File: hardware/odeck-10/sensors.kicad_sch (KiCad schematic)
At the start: 0 parts

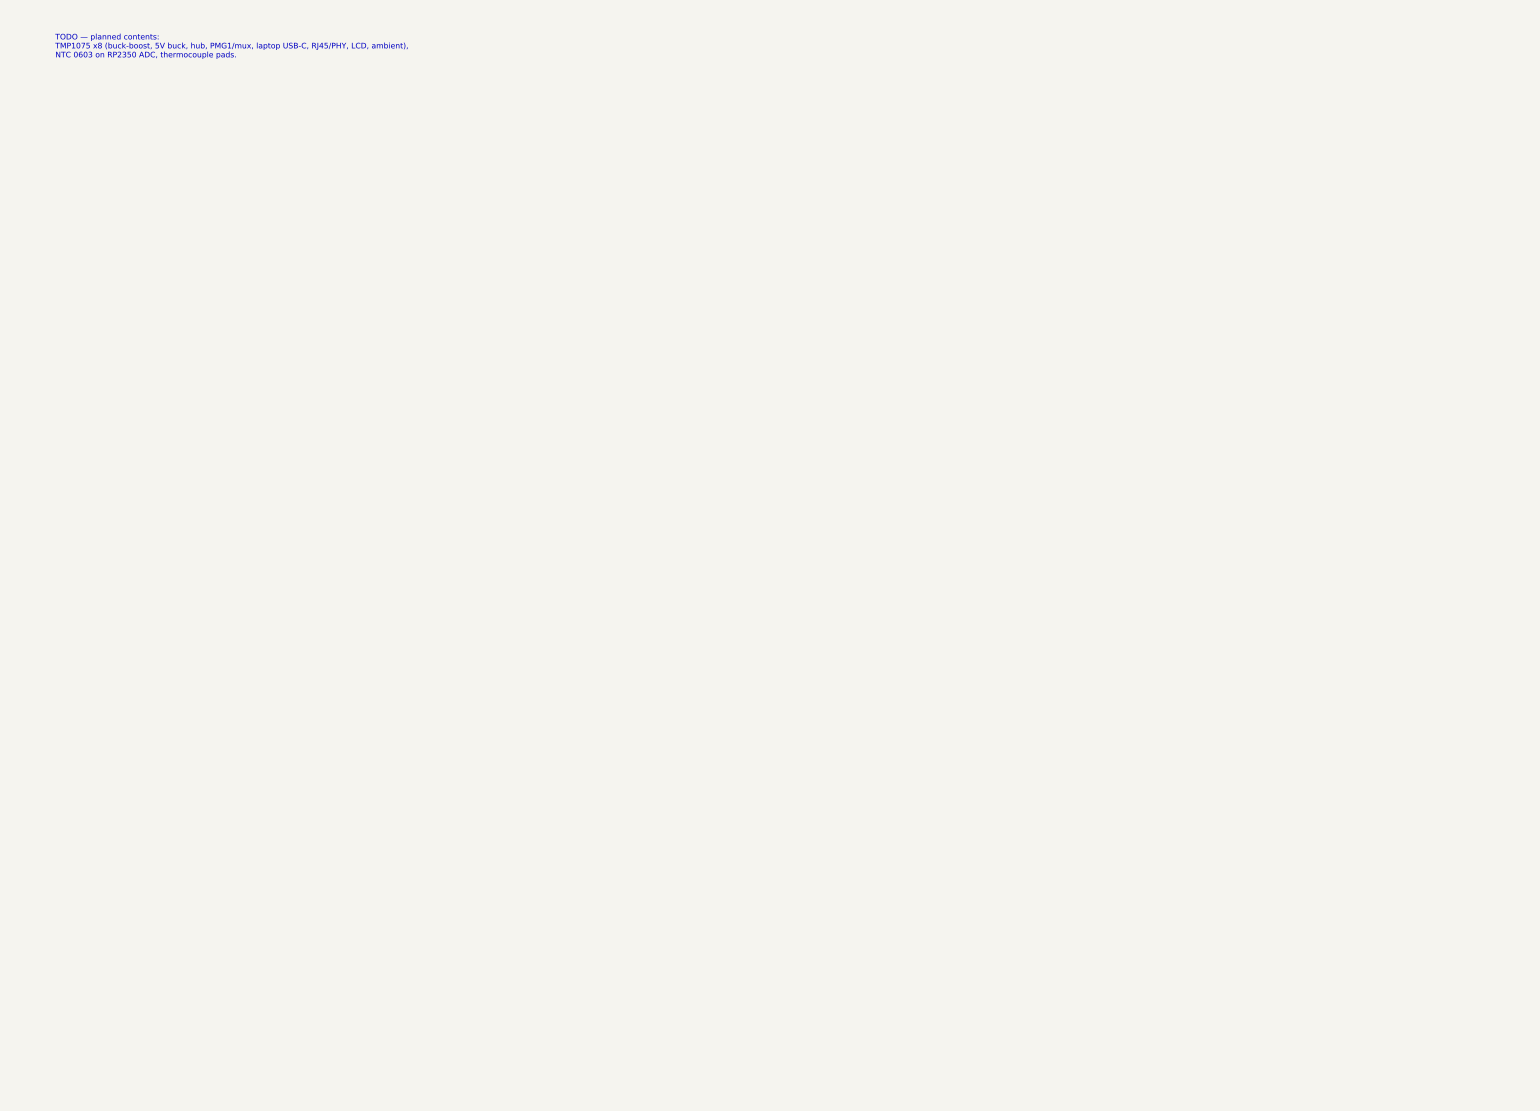
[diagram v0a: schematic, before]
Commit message: Draft remaining sheets: USB-A, card reader, Ethernet, MCU, display/UI, sensors
- usb_a: 2x 10G USB-A, TPS2553 switches (hub OR RP2350 force), INA180 sense
- card_reader: GL3224 + SD/microSD, card detect + activity to MCU
- ethernet: RTL8156BG with switched 3.3 V, 0.95 V PWM buck, 2.5G magjack,
  LED buffer, EUI-48 EEPROM + gated I2C bridge for MAC eFuse write
- mcu: RP2350B reference core, full GPIO table, TCA9534 expander, PIO I2C
- display_ui: 2.0" ST7789 LCD + backlight PWM, buttons, unpopulated GPIO
  header (series R + ESD), Qwiic
- sensors: 8x TMP1075, 2 NTCs, thermocouple pads
- integration: ETH_I2C_EN net, TPS62933F for +3V3, PWR_FLAGs
- schgen: deterministic UUIDs; bom_check: cost summary
- 181 parts, all JLC stock >= 5; netlist verify OK; ERC clean but 1 spare pin

Co-Authored-By: Claude Opus 5.5 <noreply@anthropic.com>
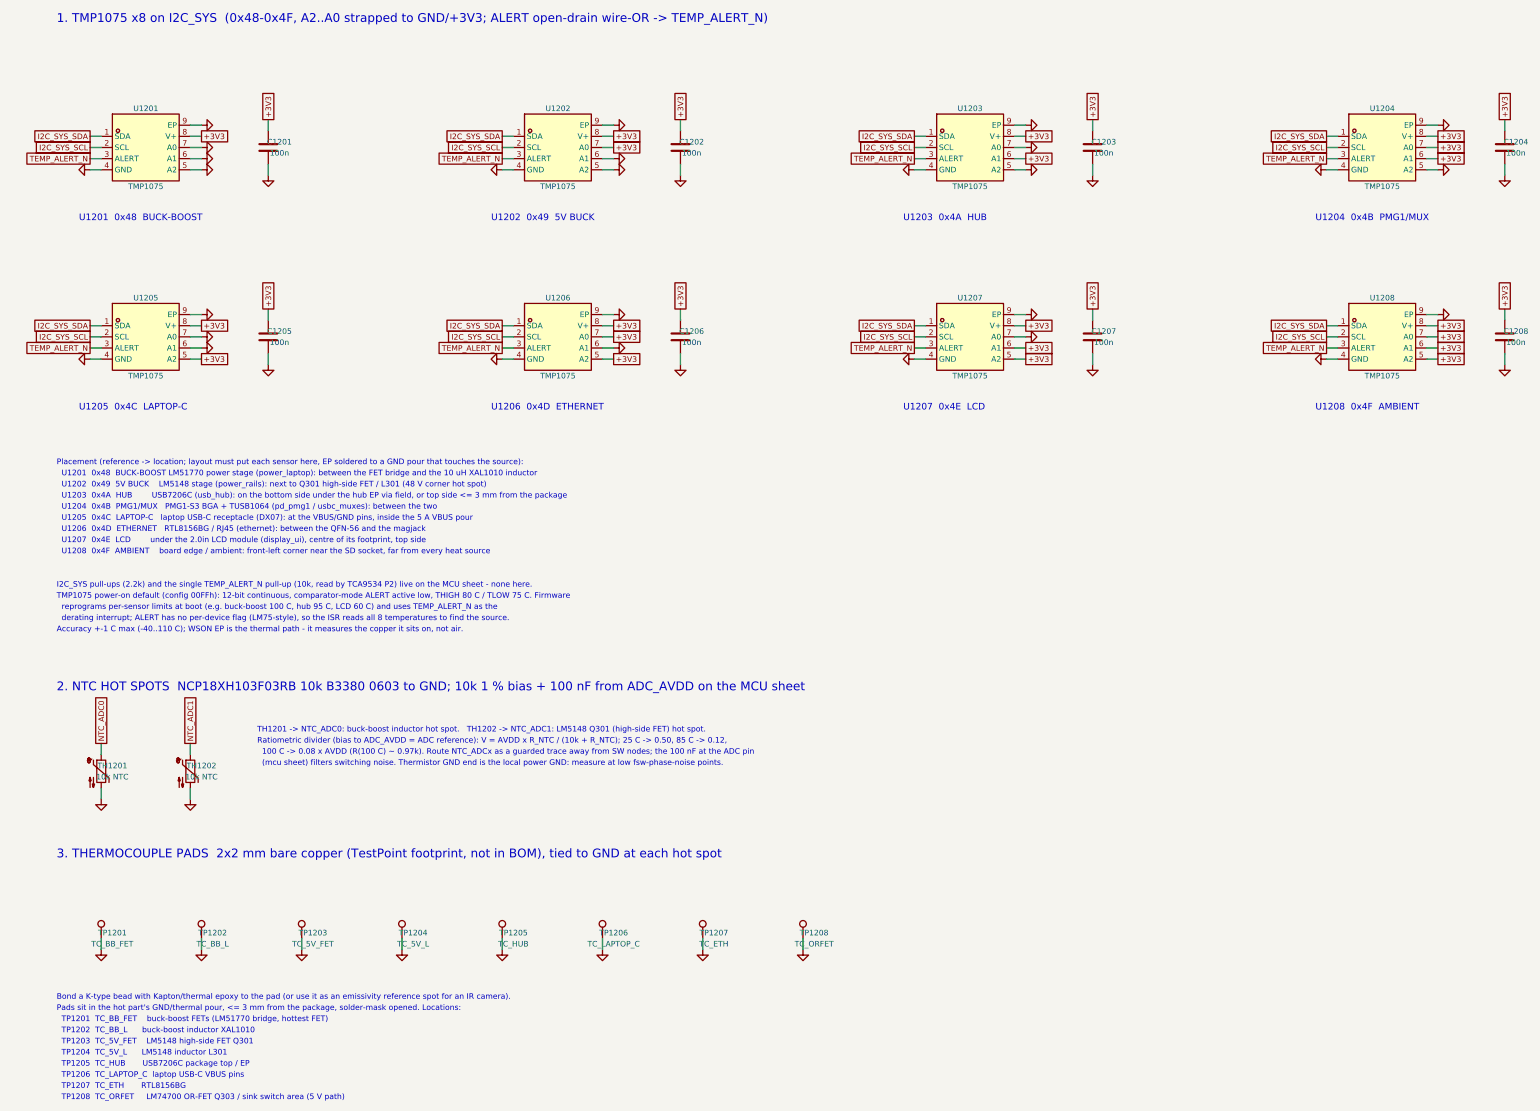
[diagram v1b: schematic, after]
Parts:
- added C1201, C1202, C1203, C1204, C1205, C1206, C1207, C1208: 100n, Capacitor_SMD:C_0402_1005Metric, symbol Device:C
- added TH1201, TH1202: 10k NTC, Resistor_SMD:R_0603_1608Metric, symbol Device:Thermistor_NTC
- added TP1201: TC_BB_FET, TestPoint:TestPoint_Pad_2.0x2.0mm, symbol Connector:TestPoint
- added TP1202: TC_BB_L, TestPoint:TestPoint_Pad_2.0x2.0mm, symbol Connector:TestPoint
- added TP1203: TC_5V_FET, TestPoint:TestPoint_Pad_2.0x2.0mm, symbol Connector:TestPoint
- added TP1204: TC_5V_L, TestPoint:TestPoint_Pad_2.0x2.0mm, symbol Connector:TestPoint
- added TP1205: TC_HUB, TestPoint:TestPoint_Pad_2.0x2.0mm, symbol Connector:TestPoint
- added TP1206: TC_LAPTOP_C, TestPoint:TestPoint_Pad_2.0x2.0mm, symbol Connector:TestPoint
- added TP1207: TC_ETH, TestPoint:TestPoint_Pad_2.0x2.0mm, symbol Connector:TestPoint
- added TP1208: TC_ORFET, TestPoint:TestPoint_Pad_2.0x2.0mm, symbol Connector:TestPoint
- added U1201, U1202, U1203, U1204, U1205, U1206, U1207, U1208: TMP1075, odeck:WSON-8_L2.0-W2.0-P0.50-TL-EP, symbol odeck:TMP1075DSGR
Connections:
- new net +3V3: C1201.1, C1202.1, C1203.1, C1204.1, C1205.1, C1206.1, C1207.1, C1208.1, U1201.8 (V+), U1202.7 (A0), U1202.8 (V+), U1203.6 (A1), U1203.8 (V+), U1204.6 (A1), U1204.7 (A0), U1204.8 (V+), U1205.5 (A2), U1205.8 (V+), U1206.5 (A2), U1206.7 (A0), U1206.8 (V+), U1207.5 (A2), U1207.6 (A1), U1207.8 (V+), U1208.5 (A2), U1208.6 (A1), U1208.7 (A0), U1208.8 (V+)
- new net GND: C1201.2, C1202.2, C1203.2, C1204.2, C1205.2, C1206.2, C1207.2, C1208.2, TH1201.2, TH1202.2, TP1201.1, TP1202.1, TP1203.1, TP1204.1, TP1205.1, TP1206.1, TP1207.1, TP1208.1, U1201.4 (GND), U1201.5 (A2), U1201.6 (A1), U1201.7 (A0), U1201.9 (EP), U1202.4 (GND), U1202.5 (A2), U1202.6 (A1), U1202.9 (EP), U1203.4 (GND), U1203.5 (A2), U1203.7 (A0), U1203.9 (EP), U1204.4 (GND), U1204.5 (A2), U1204.9 (EP), U1205.4 (GND), U1205.6 (A1), U1205.7 (A0), U1205.9 (EP), U1206.4 (GND), U1206.6 (A1), U1206.9 (EP), U1207.4 (GND), U1207.7 (A0), U1207.9 (EP), U1208.4 (GND), U1208.9 (EP)
- new net I2C_SYS_SCL: U1201.2 (SCL), U1202.2 (SCL), U1203.2 (SCL), U1204.2 (SCL), U1205.2 (SCL), U1206.2 (SCL), U1207.2 (SCL), U1208.2 (SCL)
- new net I2C_SYS_SDA: U1201.1 (SDA), U1202.1 (SDA), U1203.1 (SDA), U1204.1 (SDA), U1205.1 (SDA), U1206.1 (SDA), U1207.1 (SDA), U1208.1 (SDA)
- new net NTC_ADC0: TH1201.1
- new net NTC_ADC1: TH1202.1
- new net TEMP_ALERT_N: U1201.3 (ALERT), U1202.3 (ALERT), U1203.3 (ALERT), U1204.3 (ALERT), U1205.3 (ALERT), U1206.3 (ALERT), U1207.3 (ALERT), U1208.3 (ALERT)
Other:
- note added: "(mcu sheet) filters switching noise. Thermistor GND end is the local power GND: measure at low fsw-phase-noise points."
- note added: "1. TMP1075 x8 on I2C_SYS (0x48-0x4F, A2..A0 strapped to GND/+3V3; ALERT open-drain wire-OR -> TEMP_ALERT_N)"
- note added: "100 C -> 0.08 x AVDD (R(100 C) ~ 0.97k). Route NTC_ADCx as a guarded trace away from SW nodes; the 100 nF at the ADC pin"
- note added: "2. NTC HOT SPOTS NCP18XH103F03RB 10k B3380 0603 to GND; 10k 1 % bias + 100 nF from ADC_AVDD on the MCU sheet"
- note added: "3. THERMOCOUPLE PADS 2x2 mm bare copper (TestPoint footprint, not in BOM), tied to GND at each hot spot"
- note added: "Accuracy +-1 C max (-40..110 C); WSON EP is the thermal path - it measures the copper it sits on, not air."
- note added: "Bond a K-type bead with Kapton/thermal epoxy to the pad (or use it as an emissivity reference spot for an IR camera)."
- note added: "I2C_SYS pull-ups (2.2k) and the single TEMP_ALERT_N pull-up (10k, read by TCA9534 P2) live on the MCU sheet - none here."
- note added: "Pads sit in the hot part's GND/thermal pour, <= 3 mm from the package, solder-mask opened. Locations:"
- note added: "Placement (reference -> location; layout must put each sensor here, EP soldered to a GND pour that touches the source):"
- note added: "Ratiometric divider (bias to ADC_AVDD = ADC reference): V = AVDD x R_NTC / (10k + R_NTC); 25 C -> 0.50, 85 C -> 0.12,"
- note added: "TH1201 -> NTC_ADC0: buck-boost inductor hot spot. TH1202 -> NTC_ADC1: LM5148 Q301 (high-side FET) hot spot."
- note added: "TMP1075 power-on default (config 00FFh): 12-bit continuous, comparator-mode ALERT active low, THIGH 80 C / TLOW 75 C. Firmware"
- note added: "TP1201 TC_BB_FET buck-boost FETs (LM51770 bridge, hottest FET)"
- note added: "TP1202 TC_BB_L buck-boost inductor XAL1010"
- note added: "TP1203 TC_5V_FET LM5148 high-side FET Q301"
- note added: "TP1204 TC_5V_L LM5148 inductor L301"
- note added: "TP1205 TC_HUB USB7206C package top / EP"
- note added: "TP1206 TC_LAPTOP_C laptop USB-C VBUS pins"
- note added: "TP1207 TC_ETH RTL8156BG"
- note added: "TP1208 TC_ORFET LM74700 OR-FET Q303 / sink switch area (5 V path)"
- note added: "U1201 0x48 BUCK-BOOST"
- note added: "U1201 0x48 BUCK-BOOST LM51770 power stage (power_laptop): between the FET bridge and the 10 uH XAL1010 inductor"
- note added: "U1202 0x49 5V BUCK"
- note added: "U1202 0x49 5V BUCK LM5148 stage (power_rails): next to Q301 high-side FET / L301 (48 V corner hot spot)"
- note added: "U1203 0x4A HUB"
- note added: "U1203 0x4A HUB USB7206C (usb_hub): on the bottom side under the hub EP via field, or top side <= 3 mm from the package"
- note added: "U1204 0x4B PMG1/MUX"
- note added: "U1204 0x4B PMG1/MUX PMG1-S3 BGA + TUSB1064 (pd_pmg1 / usbc_muxes): between the two"
- note added: "U1205 0x4C LAPTOP-C"
- note added: "U1205 0x4C LAPTOP-C laptop USB-C receptacle (DX07): at the VBUS/GND pins, inside the 5 A VBUS pour"
- note added: "U1206 0x4D ETHERNET"
- note added: "U1206 0x4D ETHERNET RTL8156BG / RJ45 (ethernet): between the QFN-56 and the magjack"
- note added: "U1207 0x4E LCD"
- note added: "U1207 0x4E LCD under the 2.0in LCD module (display_ui), centre of its footprint, top side"
- note added: "U1208 0x4F AMBIENT"
- note added: "U1208 0x4F AMBIENT board edge / ambient: front-left corner near the SD socket, far from every heat source"
- note added: "derating interrupt; ALERT has no per-device flag (LM75-style), so the ISR reads all 8 temperatures to find the source."
- note added: "reprograms per-sensor limits at boot (e.g. buck-boost 100 C, hub 95 C, LCD 60 C) and uses TEMP_ALERT_N as the"
- note removed: "TODO — planned contents: TMP1075 x8 (buck-boost, 5V buck, hub, PMG1/mux, laptop USB-C, RJ45/PHY, LCD, ambient), NTC 0603 on RP2350 ADC, thermocouple pads."
- title: odeck-10 — Sensors -> odeck-10 — Thermal sensors

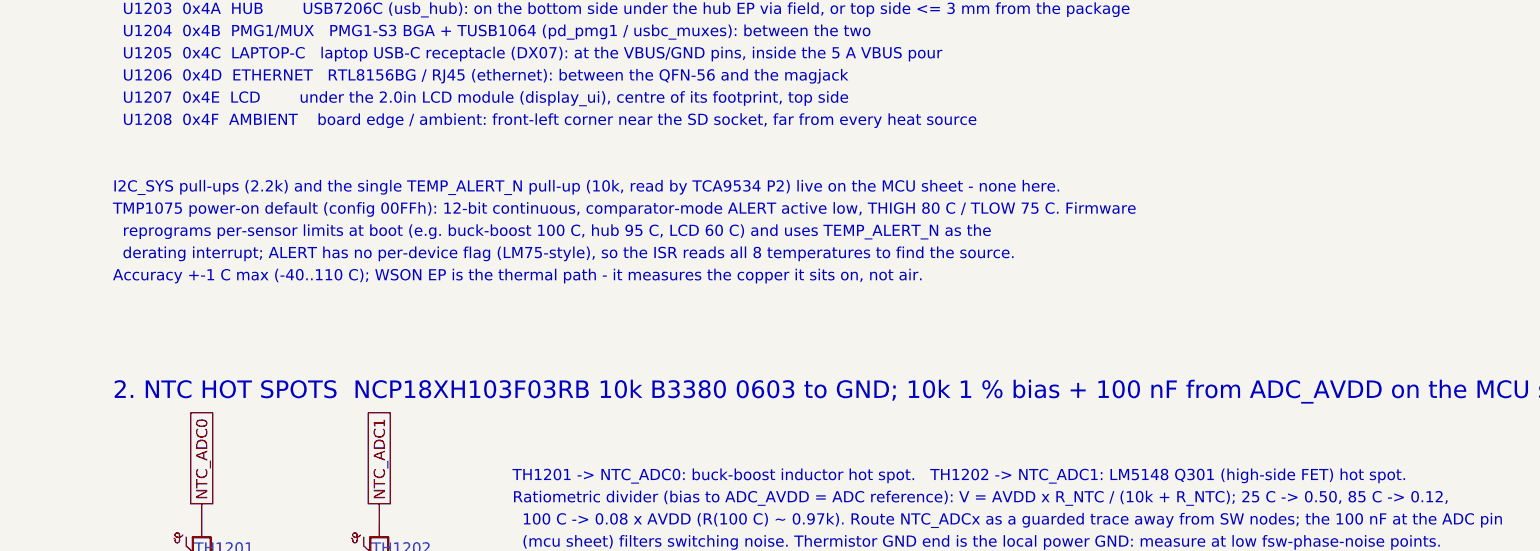
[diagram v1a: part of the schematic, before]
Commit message: Schematic review + footprint verification; fix all MAJOR findings
Reviews (docs/review/): power, PD/mux, data path, MCU/UI - 0 blockers,
7 majors, all resolved:
- power: diode-OR inputs (no shutdown-based PD-in priority), sink hand-over
  gated by delayed PG_5V, PD-in capacitance within 100 uF, HV resistor sizes,
  OVP filter/threshold, VBB_PG soft-start qualification
- card reader MS2_INS/SD2_WP phantom card, hub VBUS_DET level buffer
- RP2350 inductor dot text; minors across all sheets (HPD pull-down, PMG1
  INT pin, PHY TX caps, erratum E9 pull-downs, PHY I2C bridge gating,
  backlight 39 ohm, +1V1 cap, IOX P7)
Footprints: all 54 custom footprints checked vs manufacturer drawings,
50 fixed (courtyards, pads, paste, RJ45 mirrored pinout, EP sizes, holes);
removed obsolete FL_001 placeholder.
Firmware rules collected in docs/design/mcu.md.
186 parts, all JLC stock >= 5; netlist verify OK; ERC clean.

Co-Authored-By: Claude Opus 5.5 <noreply@anthropic.com>
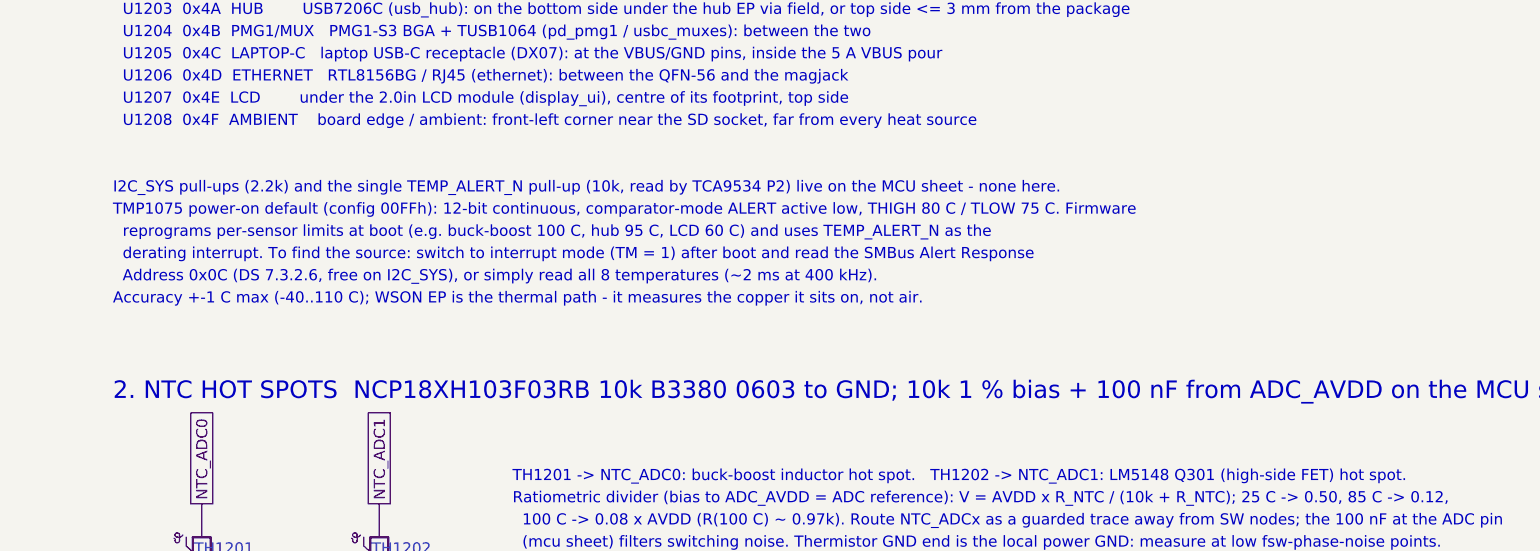
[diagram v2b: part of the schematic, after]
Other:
- note added: "Address 0x0C (DS 7.3.2.6, free on I2C_SYS), or simply read all 8 temperatures (~2 ms at 400 kHz)."
- note added: "derating interrupt. To find the source: switch to interrupt mode (TM = 1) after boot and read the SMBus Alert Response"
- note removed: "derating interrupt; ALERT has no per-device flag (LM75-style), so the ISR reads all 8 temperatures to find the source."
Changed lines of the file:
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@@
 		)
 	)
-	(text "  derating interrupt; ALERT has no per-device flag (LM75-style), so the ISR reads all 8 temperatures to find the source."
+	(text "  derating interrupt. To find the source: switch to interrupt mode (TM = 1) after boot and read the SMBus Alert Response"
 		(exclude_from_sim no)
 		(at 20.32 152.4 0)
@@
 		)
 	)
-	(text "Accuracy +-1 C max (-40..110 C); WSON EP is the thermal path - it measures the copper it sits on, not air."
+	(text "  Address 0x0C (DS 7.3.2.6, free on I2C_SYS), or simply read all 8 temperatures (~2 ms at 400 kHz)."
 		(exclude_from_sim no)
 		(at 20.32 154.94 0)
 		(effects
 			(font
+				(size 1.27 1.27)
+			)
+			(justify left top)
+		)
+	)
+	(text "Accuracy +-1 C max (-40..110 C); WSON EP is the thermal path - it measures the copper it sits on, not air."
+		(exclude_from_sim no)
+		(at 20.32 157.48 0)
+		(effects
+			(font
